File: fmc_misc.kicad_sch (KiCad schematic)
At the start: 14 parts, among them J1501 10029449-111RLF, J1502 PPPC072LJBN-RC, J1503 PPPC072LJBN-RC, Q1501 FDN335N, Q1502 FDN335N

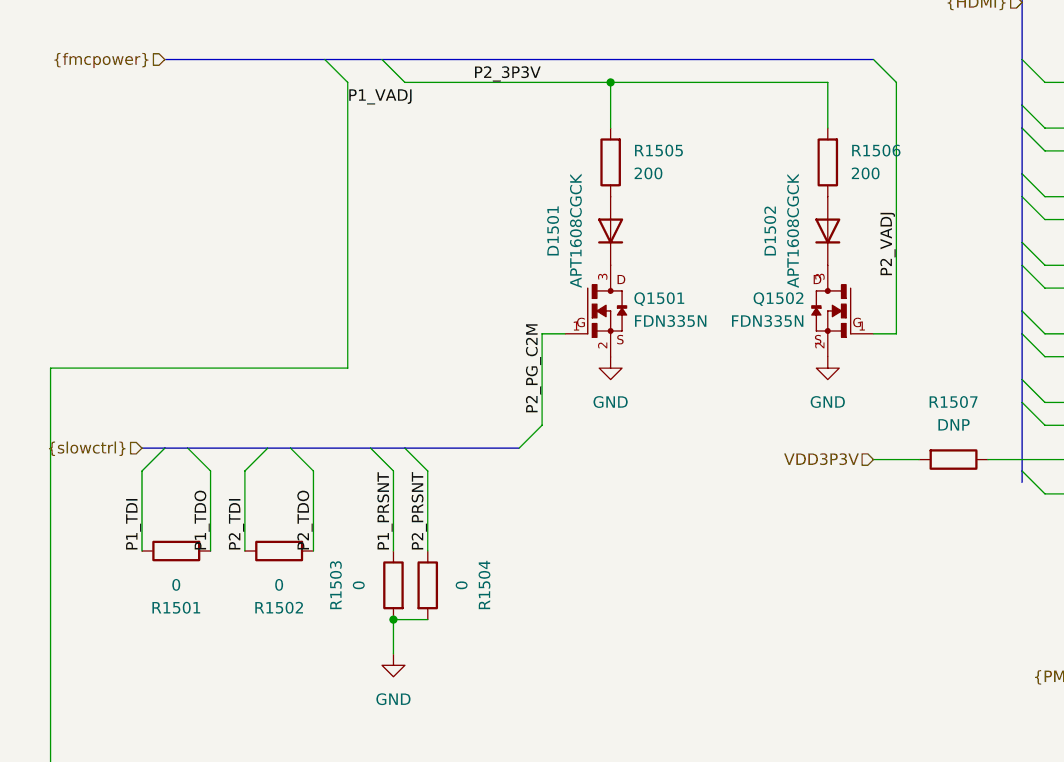
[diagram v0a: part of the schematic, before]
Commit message: Schematic Changes
Added Manufacturer/MPN/Description Fields to parts
Added libraries to project
Modified FMC schematic to use new symbol
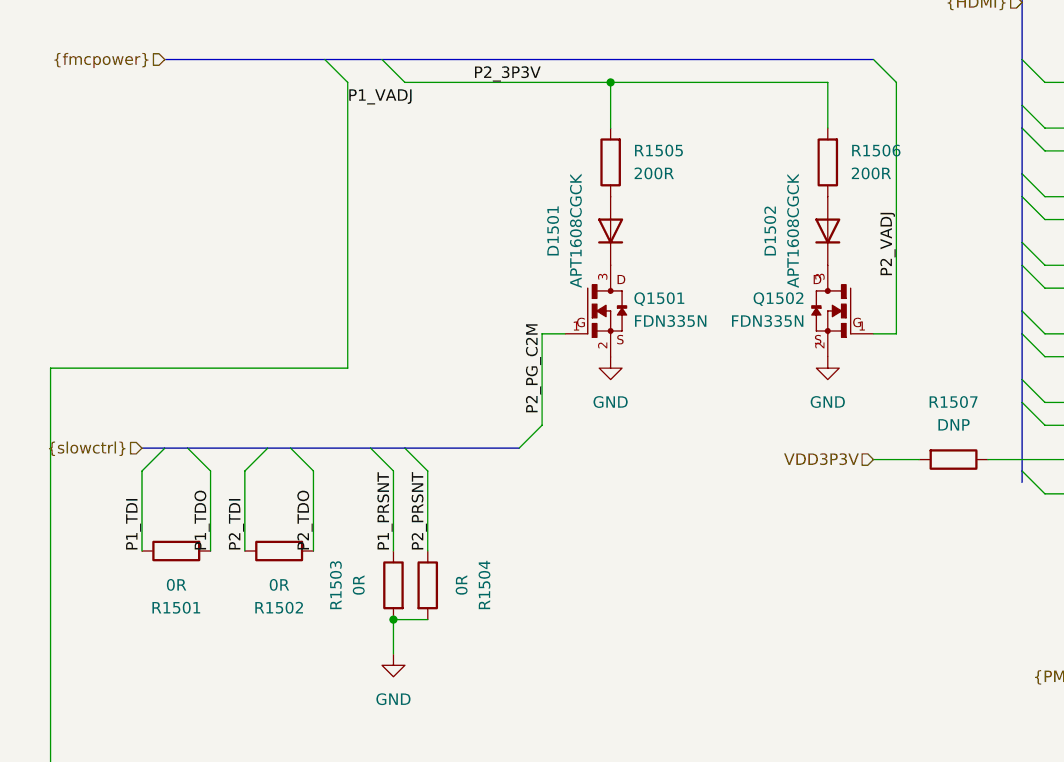
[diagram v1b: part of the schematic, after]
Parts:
- D1501, D1502: Manufacturer (none) -> Kingbright; Manufacturer Part Number (none) -> APT1608CGCK
- J1501: Manufacturer (none) -> Amphenol; Manufacturer Part Number (none) -> 10029449-111RLF
- J1502, J1503: Manufacturer (none) -> Sullins; Manufacturer Part Number (none) -> PPPC072LJBN-RC
- Q1501, Q1502: Manufacturer (none) -> onsemi; Manufacturer Part Number (none) -> FDN335N
- R1501, R1502, R1503, R1504: value 0 -> 0R; Manufacturer (none) -> Panasonic; Manufacturer Part Number (none) -> ERJ-3GEY0R00V
- R1505, R1506: value 200 -> 200R; Manufacturer (none) -> Susumu; Manufacturer Part Number (none) -> RR0816P-201-D

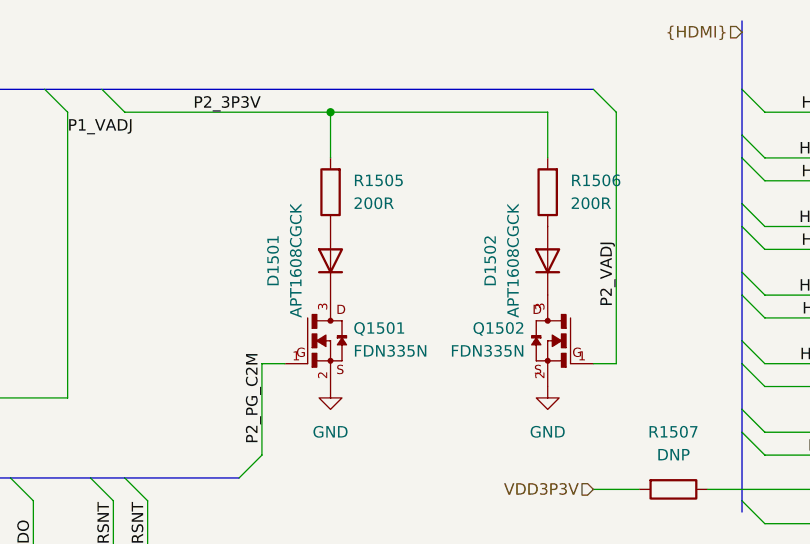
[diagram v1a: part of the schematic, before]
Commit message: Updated some Schematics
- updated slowmon schematic
- updated diff to se schematic
- cleaned up DRC/ERC errors
No changes were made that effected the PCB layout
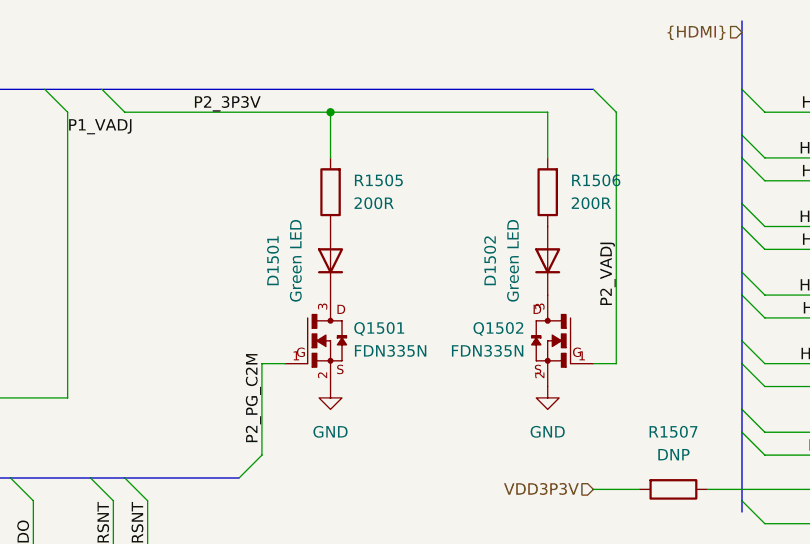
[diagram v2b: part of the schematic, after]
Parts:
- D1501, D1502: value APT1608CGCK -> Green LED
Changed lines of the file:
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@@
 			)
 		)
-		(property "Value" "APT1608CGCK"
+		(property "Value" "Green LED"
 			(at 80.01 58.42 0)
 			(effects
@@
 			)
 		)
-		(property "Value" "APT1608CGCK"
+		(property "Value" "Green LED"
 			(at 104.14 58.42 0)
 			(effects

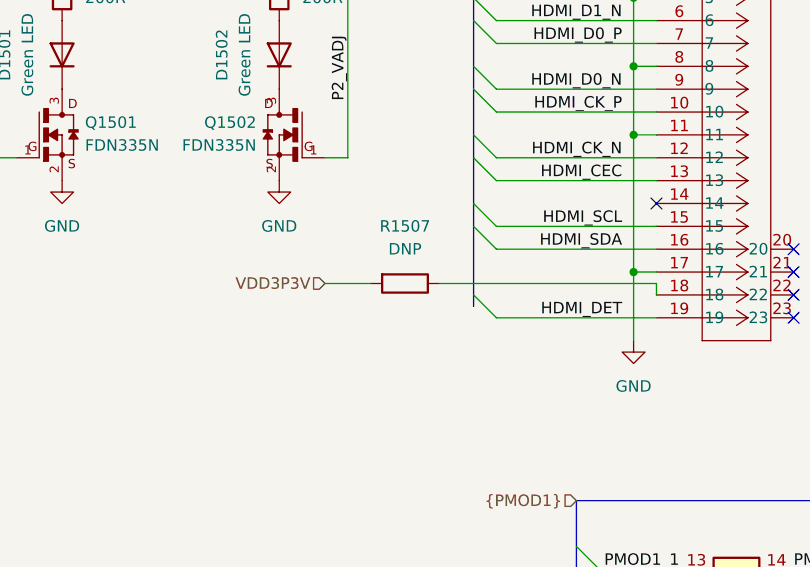
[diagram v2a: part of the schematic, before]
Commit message: Properly attributed DNP parts; Added Fabrication Notes
-Properly attributed various DNP in the project;
This includes: C210.C710,C1601,C2502,C2602,L2501,R1507,L2601,R1601,R805
- I changed the accelerometer and microphone (+it's filter)to DNP parts
  Note: both of these are obsolete parts. As part of this change I Changed R1602 (part of mic buffer) from 220k to 0R. The removal of these parts should in no way negatively effect the rest of the circuit.
-I fixed the 'value' attribute of XMER2501&XMER2601 from 'TC4-6+' -> 'TC4-6T+'
- I added some fabrication notes to the F.Fab Layer
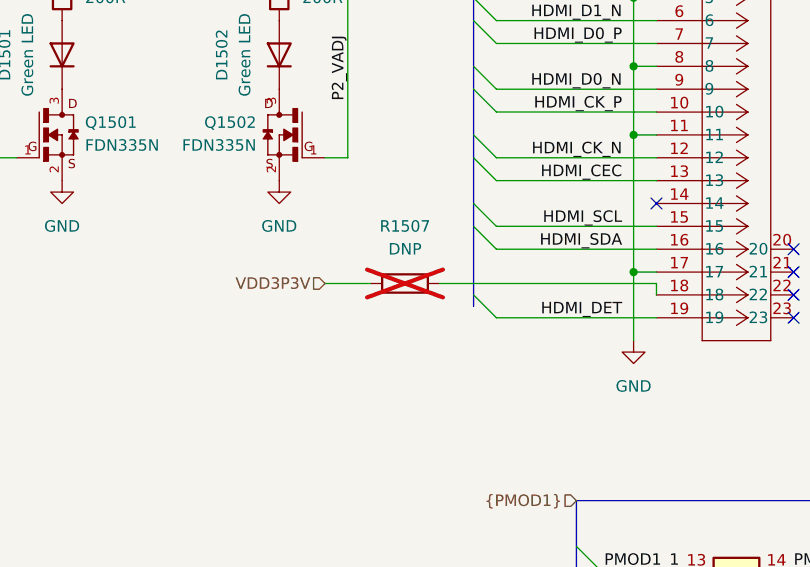
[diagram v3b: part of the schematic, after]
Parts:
- R1507: now not fitted
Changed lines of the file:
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@@
 		(in_bom yes)
 		(on_board yes)
-		(dnp no)
+		(dnp yes)
 		(fields_autoplaced yes)
 		(property "Reference" "R1507"
